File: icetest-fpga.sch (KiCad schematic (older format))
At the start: 13 parts

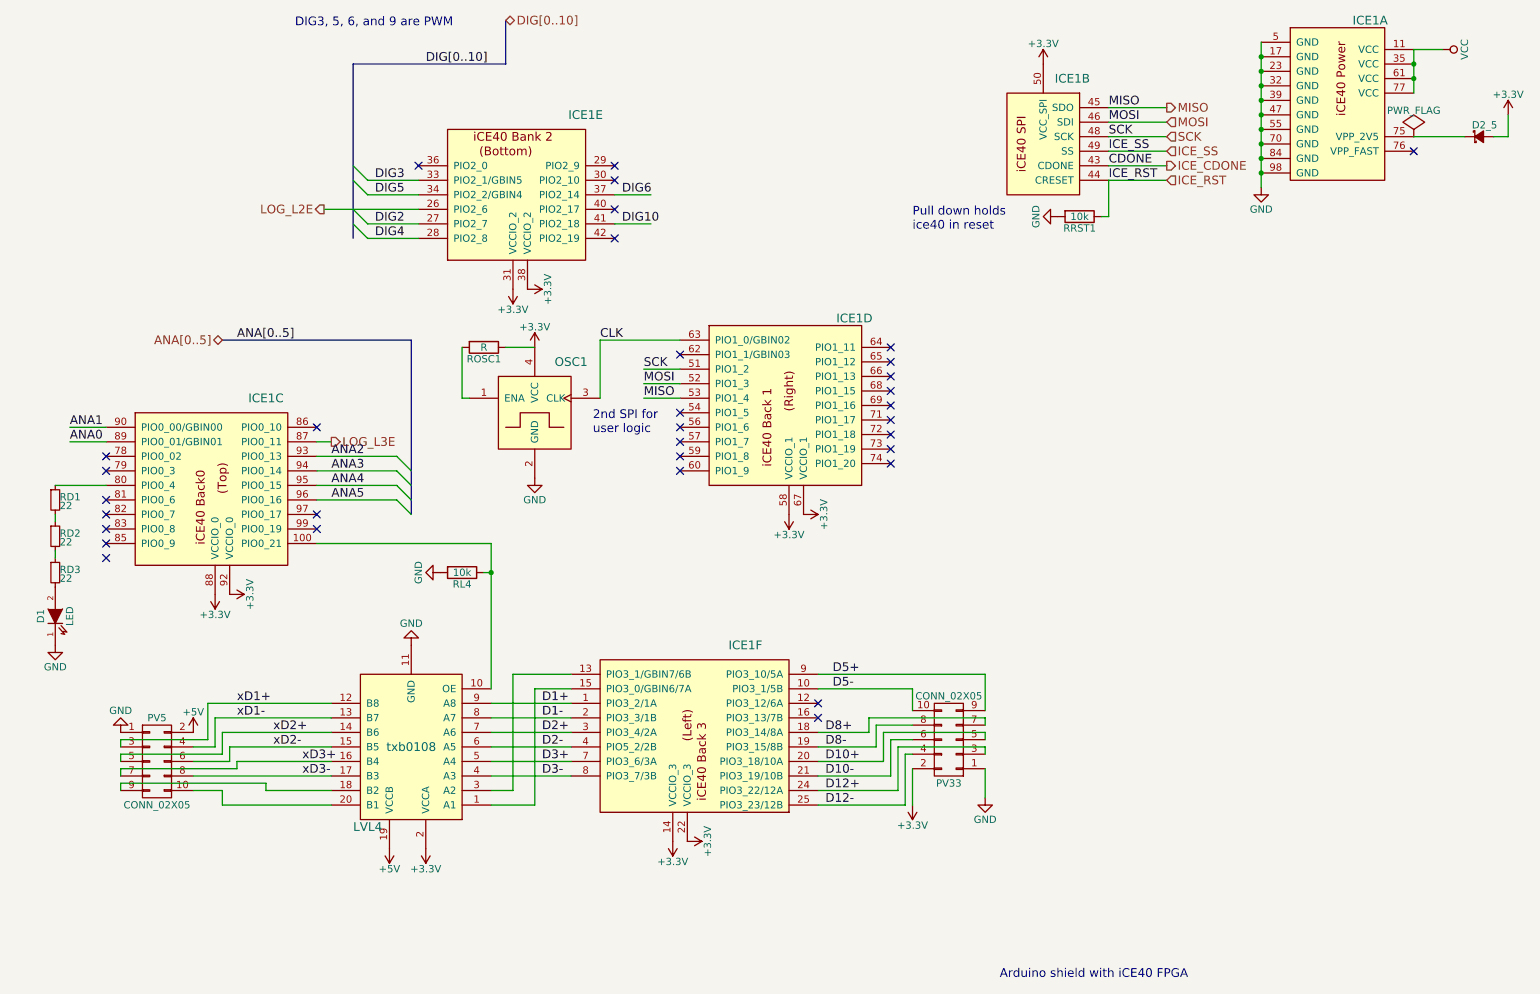
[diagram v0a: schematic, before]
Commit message: add SPI test points and verify footprints
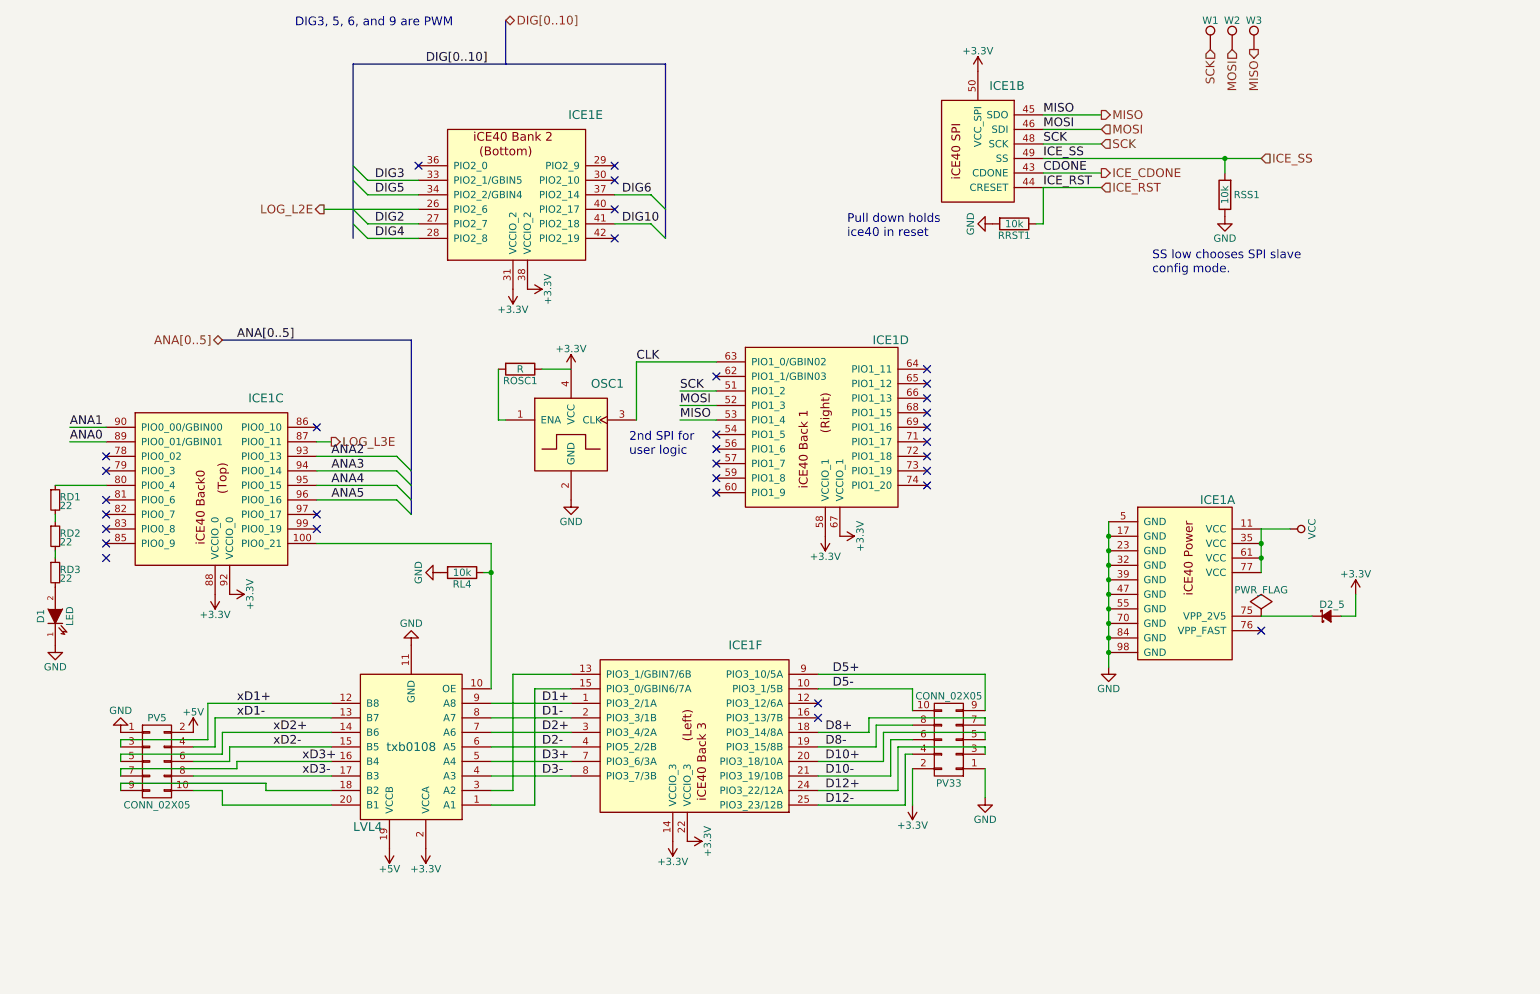
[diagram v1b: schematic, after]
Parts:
- added RSS1: 10k, Resistors_SMD:R_0603_HandSoldering, symbol R
- added W1, W2, W3: TEST_1P, Connect:PINTST, symbol TEST_1P
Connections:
- net GND: now also RSS1.1
- net ICE_SS: now also RSS1.2
- net MISO: now also W3.1
- net MOSI: now also W2.1
- net SCK: now also W1.1
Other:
- note added: "SS low chooses SPI slave\nconfig mode."
- note removed: "Arduino shield with iCE40 FPGA"
- moved on the sheet: D2_5, ICE1A, ICE1B, ICE1D, OSC1, ROSC1, RRST1

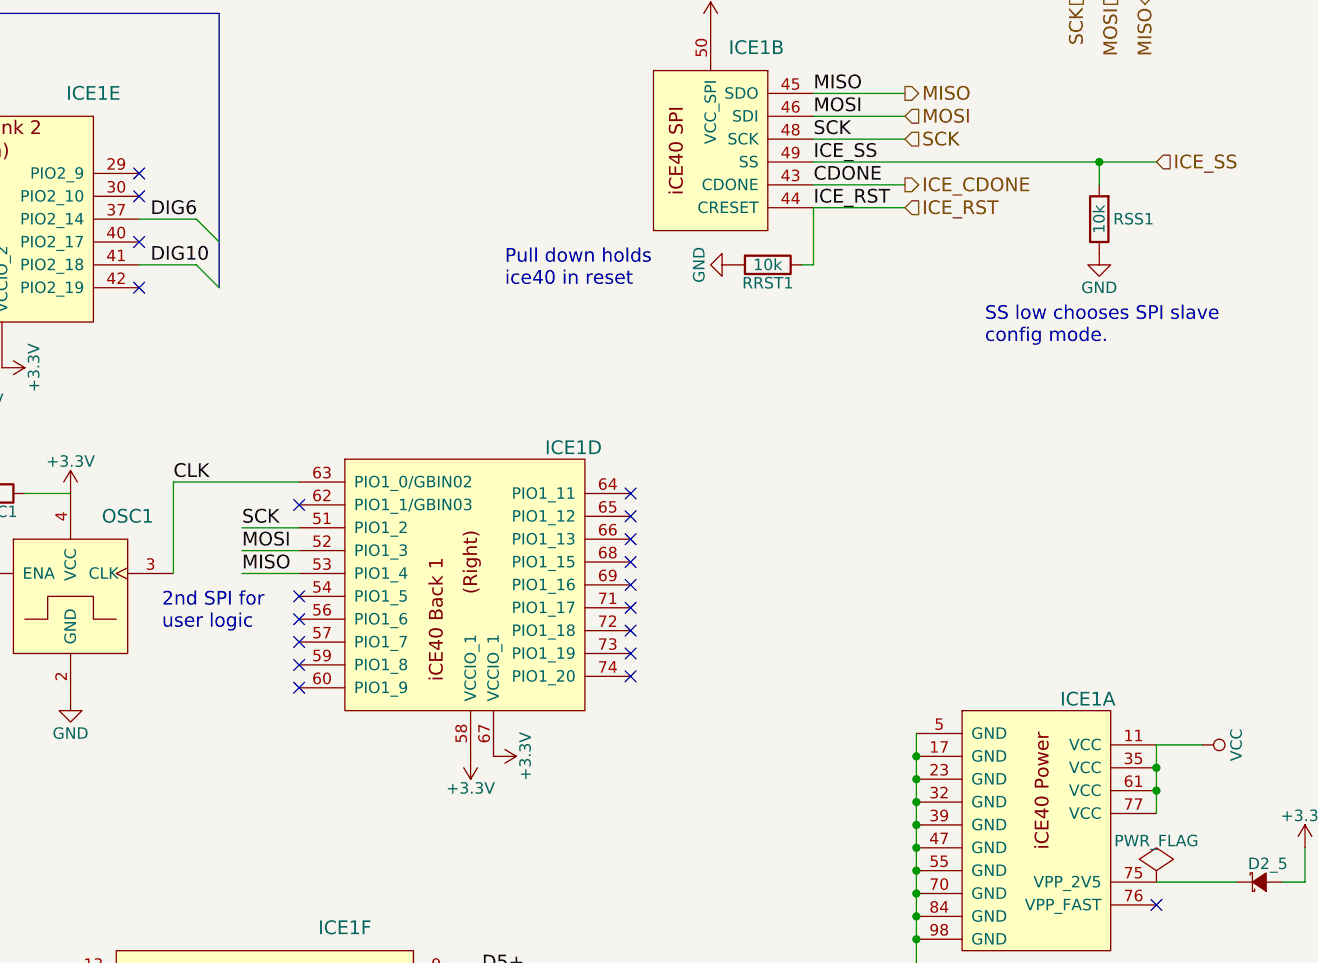
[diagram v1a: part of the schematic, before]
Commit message: fix ard symbol and route
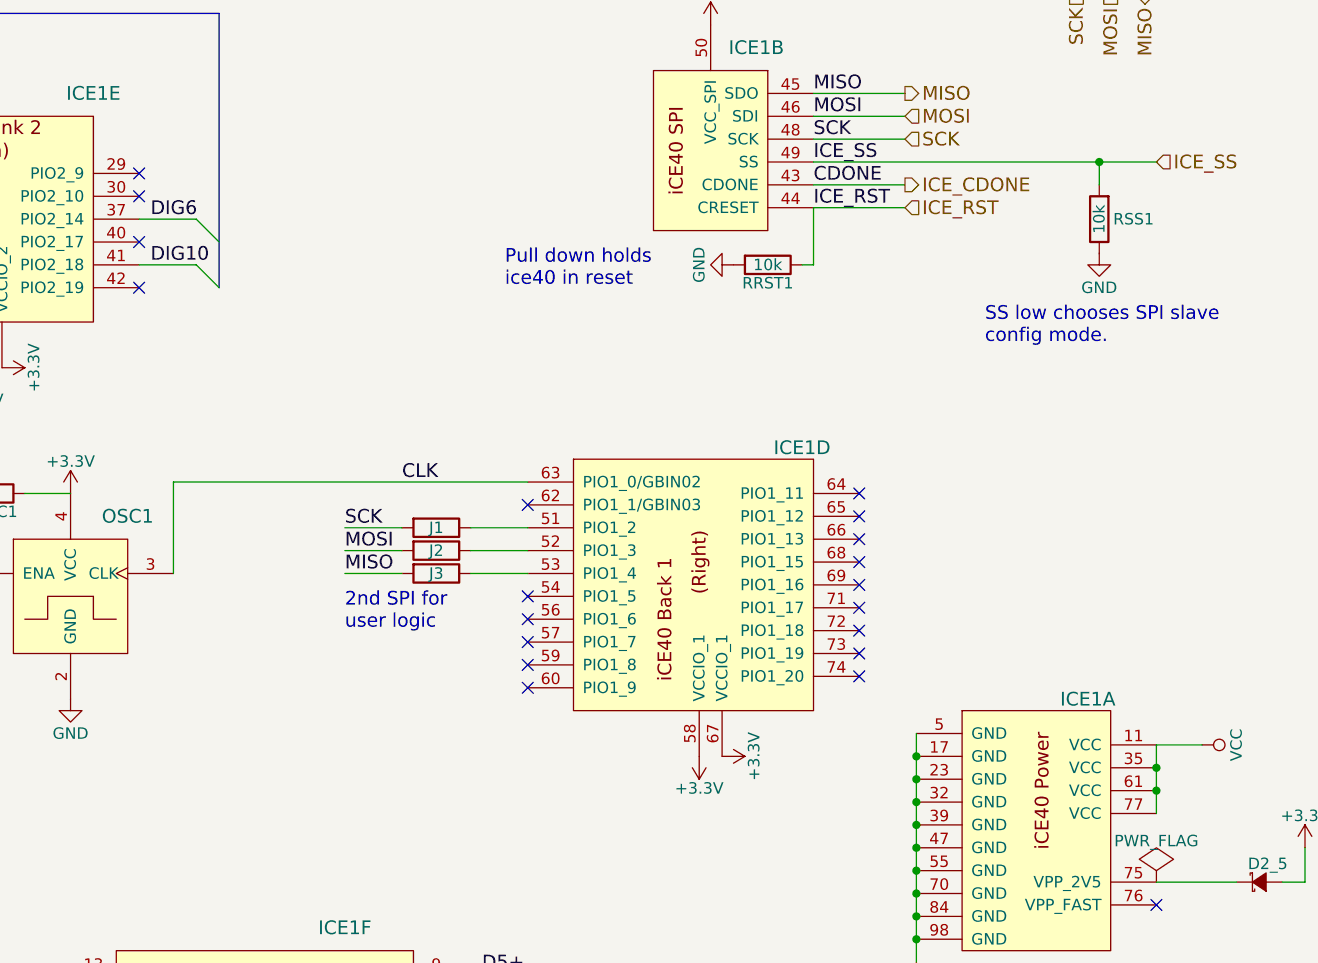
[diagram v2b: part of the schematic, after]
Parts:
- added J1, J2, J3: R, Resistors_SMD:R_0603_HandSoldering, symbol R
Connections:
- net MISO: now also J3.2; no longer ICE1.53 (PIO1_4)
- net MOSI: now also J2.2; no longer ICE1.52 (PIO1_3)
- net SCK: now also J1.2; no longer ICE1.51 (PIO1_2)
- new net: ICE1.51 (PIO1_2), J1.1
- new net: ICE1.52 (PIO1_3), J2.1
- new net: ICE1.53 (PIO1_4), J3.1
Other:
- moved on the sheet: ICE1D
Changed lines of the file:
@@
 	1    0    0    -1
 $EndComp
-Text Label 4850 3250 0    60   ~ 0
+Text Label 5850 3250 0    60   ~ 0
 CLK
 $Comp
@@
 L +3.3V #PWR064
 U 1 1 578BBABE
-P 6250 4450
-F 0 "#PWR064" H 6250 4300 50  0001 C CNN
-F 1 "+3.3V" H 6250 4590 50  0000 C CNN
-F 2 "" H 6250 4450 50  0000 C CNN
-F 3 "" H 6250 4450 50  0000 C CNN
-	1    6250 4450
+P 7250 4450
+F 0 "#PWR064" H 7250 4300 50  0001 C CNN
+F 1 "+3.3V" H 7250 4590 50  0000 C CNN
+F 2 "" H 7250 4450 50  0000 C CNN
+F 3 "" H 7250 4450 50  0000 C CNN
+	1    7250 4450
 	0    1    1    0
 $EndComp
@@
 L +3.3V #PWR065
 U 1 1 578BBAEA
-P 6150 4450
-F 0 "#PWR065" H 6150 4300 50  0001 C CNN
-F 1 "+3.3V" H 6150 4590 50  0000 C CNN
-F 2 "" H 6150 4450 50  0000 C CNN
-F 3 "" H 6150 4450 50  0000 C CNN
-	1    6150 4450
+P 7150 4450
+F 0 "#PWR065" H 7150 4300 50  0001 C CNN
+F 1 "+3.3V" H 7150 4590 50  0000 C CNN
+F 2 "" H 7150 4450 50  0000 C CNN
+F 3 "" H 7150 4450 50  0000 C CNN
+	1    7150 4450
 	-1   0    0    1
 $EndComp
@@
 	7650 1750 8050 1750
 Wire Wire Line
-	9150 1850 7650 1850
+	7650 1850 9150 1850
 Wire Wire Line
 	7650 1950 8050 1950
@@
 	3900 3650 3950 3650
 Wire Wire Line
-	5400 3250 4850 3250
+	6400 3250 4850 3250
 Wire Wire Line
 	4850 3250 4850 3650
@@
 NoConn ~ 6100 5600
 NoConn ~ 6100 5700
-NoConn ~ 5400 3750
-NoConn ~ 5400 3850
-NoConn ~ 5400 3950
-NoConn ~ 5400 4050
-NoConn ~ 5400 4150
-NoConn ~ 6850 4100
-NoConn ~ 6850 4000
-NoConn ~ 6850 3900
-NoConn ~ 6850 3800
-NoConn ~ 6850 3700
-NoConn ~ 6850 3600
-NoConn ~ 6850 3500
-NoConn ~ 6850 3400
-NoConn ~ 6850 3300
+NoConn ~ 6400 3750
+NoConn ~ 6400 3850
+NoConn ~ 6400 3950
+NoConn ~ 6400 4050
+NoConn ~ 6400 4150
+NoConn ~ 7850 4100
+NoConn ~ 7850 4000
+NoConn ~ 7850 3900
+NoConn ~ 7850 3800
+NoConn ~ 7850 3700
+NoConn ~ 7850 3600
+NoConn ~ 7850 3500
+NoConn ~ 7850 3400
+NoConn ~ 7850 3300
 NoConn ~ 3350 1900
 NoConn ~ 4700 1900
@@
 	2000 6200 1800 6200
 Wire Wire Line
-	5400 3450 5150 3450
-Wire Wire Line
-	5400 3550 5150 3550
-Wire Wire Line
-	5400 3650 5150 3650
-Text Label 5150 3450 0    60   ~ 0
+	6150 3450 6400 3450
+Wire Wire Line
+	6150 3550 6400 3550
+Wire Wire Line
+	6150 3650 6400 3650
+Text Label 5600 3450 0    60   ~ 0
 SCK
-Text Label 5150 3550 0    60   ~ 0
+Text Label 5600 3550 0    60   ~ 0
 MOSI
-Text Label 5150 3650 0    60   ~ 0
+Text Label 5600 3650 0    60   ~ 0
 MISO
-Text Notes 4800 3900 0    60   ~ 0
+Text Notes 5600 3900 0    60   ~ 0
 2nd SPI for\nuser logic
 $Comp
 L iCE40HX1K-VQ100 ICE1
 U 4 1 578D5952
-P 6150 3700
-F 0 "ICE1" H 6600 4300 60  0000 C CNN
-F 1 "iCE40HX1K-VQ100" H 6150 4500 60  0001 C CNN
-F 2 "local:VQFP-100" H 6400 3800 60  0001 C CNN
-F 3 "" H 6400 3800 60  0000 C CNN
-	4    6150 3700
+P 7150 3700
+F 0 "ICE1" H 7600 4300 60  0000 C CNN
+F 1 "iCE40HX1K-VQ100" H 7150 4500 60  0001 C CNN
+F 2 "local:VQFP-100" H 7400 3800 60  0001 C CNN
+F 3 "" H 7400 3800 60  0000 C CNN
+	4    7150 3700
 	1    0    0    -1
 $EndComp
@@
 Wire Wire Line
 	4700 2300 4950 2300
-NoConn ~ 5400 3350
+NoConn ~ 6400 3350
 NoConn ~ 1200 4400
 Wire Wire Line
@@
 Entry Wire Line
 	4950 2300 5050 2400
+$Comp
+L R J1
+U 1 1 5796B92D
+P 6000 3450
+F 0 "J1" V 6000 3450 50  0000 C CNN
+F 1 "R" H 6000 3450 50  0001 C CNN
+F 2 "Resistors_SMD:R_0603_HandSoldering" V 5930 3450 50  0001 C CNN
+F 3 "" H 6000 3450 50  0000 C CNN
+	1    6000 3450
+	0    1    1    0
+$EndComp
+$Comp
+L R J2
+U 1 1 5796BB7A
+P 6000 3550
+F 0 "J2" V 6000 3550 50  0000 C CNN
+F 1 "R" H 6000 3550 50  0001 C CNN
+F 2 "Resistors_SMD:R_0603_HandSoldering" V 5930 3550 50  0001 C CNN
+F 3 "" H 6000 3550 50  0000 C CNN
+	1    6000 3550
+	0    1    1    0
+$EndComp
+$Comp
+L R J3
+U 1 1 5796BBD2
+P 6000 3650
+F 0 "J3" V 6000 3650 50  0000 C CNN
+F 1 "R" H 6000 3650 50  0001 C CNN
+F 2 "Resistors_SMD:R_0603_HandSoldering" V 5930 3650 50  0001 C CNN
+F 3 "" H 6000 3650 50  0000 C CNN
+	1    6000 3650
+	0    1    1    0
+$EndComp
+Wire Wire Line
+	5850 3450 5600 3450
+Wire Wire Line
+	5600 3550 5850 3550
+Wire Wire Line
+	5850 3650 5600 3650
 $EndSCHEMATC

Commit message: remove dup pins from symbols
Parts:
- ICE1: symbol iCE40HX1K-VQ100-RESCUE-icetest -> iCE40HX1K-VQ100
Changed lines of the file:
@@
 NoConn ~ 9150 5100
 $Comp
-L iCE40HX1K-VQ100-RESCUE-icetest ICE1
+L iCE40HX1K-VQ100 ICE1
 U 1 1 578C5D61
 P 8600 4750
